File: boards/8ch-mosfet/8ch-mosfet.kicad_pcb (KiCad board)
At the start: 2 copper layers, 184.5 x 137 mm, 193 parts, among them J10 Screw_Terminal_01x02, J11 Screw_Terminal_01x02, J12 Screw_Terminal_01x02, J13 I2C, J14 N2K, J3 Screw_Terminal_01x08, J5 Screw_Terminal_01x02, J6 Screw_Terminal_01x02, J7 Screw_Terminal_01x02, J8 Screw_Terminal_01x02, J9 Screw_Terminal_01x02, M1 Fan_4pin, M2 Fan_4pin, Q1 2N7002, Q10 IRF4905, Q11 2N7002, Q12 IRF4905, Q13 2N7002, Q14 IRF4905, Q15 2N7002, Q16 IRF4905, Q2 IRF4905, Q3 2N7002, Q4 IRF4905, Q5 2N7002, Q6 IRF4905, Q7 2N7002, Q8 IRF4905, Q9 2N7002, U1 ESP32-DEVKITC, U10 ACS725xLCTR-20AU, U11 ACS725xLCTR-20AU, U12 ACS725xLCTR-20AU, U13 MCP1502, U2 MCP3208, U3 R-78K5.0-1.0, U4 MCP3221A0T, U5 ACS725xLCTR-20AU, U6 ACS725xLCTR-20AU, U7 ACS725xLCTR-20AU, U8 ACS725xLCTR-20AU, U9 ACS725xLCTR-20AU

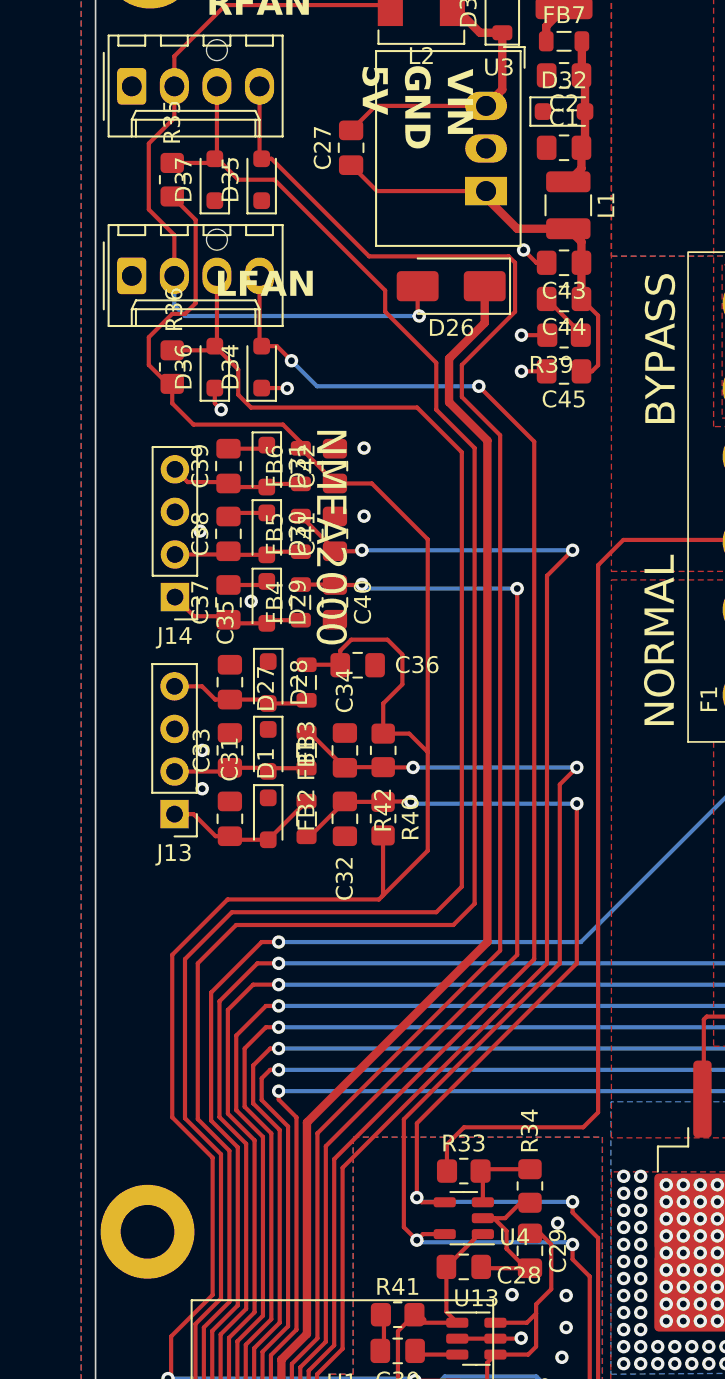
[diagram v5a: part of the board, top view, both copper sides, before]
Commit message: added in reverse polarity diode to power circuit
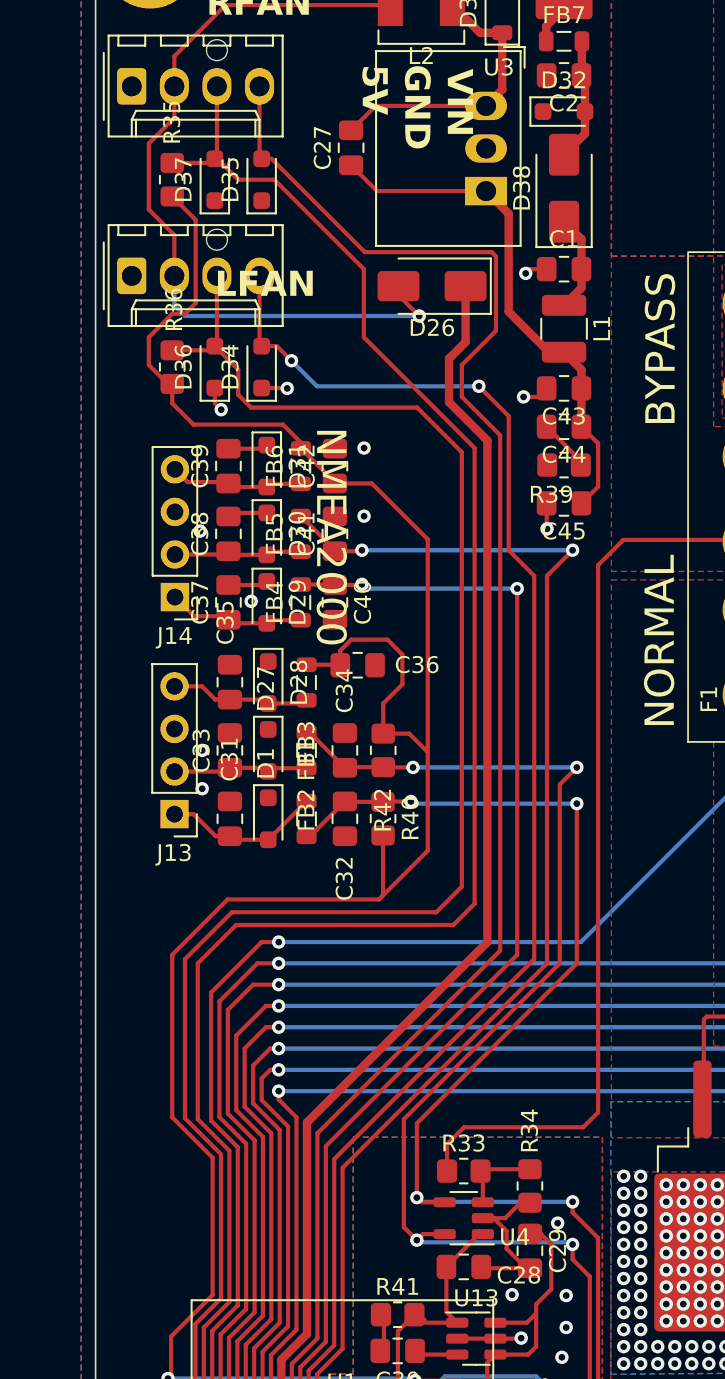
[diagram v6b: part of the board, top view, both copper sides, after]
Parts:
- removed the REF** at (3.10, 79.0)
- added D38: SX33L, Diode_SMD:D_SMA, F.Cu at (27.9, 16.8)
- moved C45 7.87 mm to (27.9, 35.6)
- moved R39 7.75 mm to (27.9, 33.3)
- moved C44 7.62 mm to (27.9, 31.0)
- moved C43 7.49 mm to (27.9, 28.7)
- moved L1 7.37 mm to (27.9, 25.1)
- moved C1 7.24 mm to (27.9, 21.6)
- moved D26 1.14 mm to (20.1, 22.6)
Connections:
- C1 pad 1: Net-(D32-A2) -> Net-(D38-K)
- L1 pad 1: Net-(D32-A2) -> Net-(D38-K)
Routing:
- net Net-(U3-IN): track 24.8 -> 31.4 mm
- net Net-(D38-K): track 0.00 -> 5.84 mm
- net Net-(D32-A2): track 8.89 -> 7.38 mm
- net FAN_PWM2: track 147.6 -> 146.2 mm
